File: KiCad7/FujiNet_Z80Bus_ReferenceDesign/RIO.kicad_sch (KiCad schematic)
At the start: 17 parts, among them IC1 7432N, IC2 7404N, IC4 7408N, IC8 7432N, IC9 7408N

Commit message: KiCAD attempt to route a single board (failed)
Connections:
- net DEC14: now also RN1.5; no longer RN1.2
- net DEC15: now also RN1.4; no longer RN1.3
- net DEC_OE: now also RN1.2; no longer RN1.5
- net DEC_WE: now also RN1.3; no longer RN1.4
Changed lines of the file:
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@@
     (effects (font (size 1.27 1.27)) (justify left bottom))
   )
-  (label "DEC_WE" (at 138.43 172.72 180) (fields_autoplaced)
+  (label "DEC_WE" (at 138.43 170.18 180) (fields_autoplaced)
     (effects (font (size 1.27 1.27)) (justify right bottom))
   )
@@
     (effects (font (size 1.27 1.27)) (justify left bottom))
   )
-  (label "DEC15" (at 138.43 170.18 180) (fields_autoplaced)
+  (label "DEC15" (at 138.43 172.72 180) (fields_autoplaced)
     (effects (font (size 1.27 1.27)) (justify right bottom))
   )
@@
     (effects (font (size 1.27 1.27)) (justify right bottom))
   )
-  (label "DEC_OE" (at 138.43 175.26 180) (fields_autoplaced)
+  (label "DEC_OE" (at 138.43 167.64 180) (fields_autoplaced)
     (effects (font (size 1.27 1.27)) (justify right bottom))
   )
@@
     (effects (font (size 1.27 1.27)) (justify left bottom))
   )
-  (label "DEC14" (at 138.43 167.64 180) (fields_autoplaced)
+  (label "DEC14" (at 138.43 175.26 180) (fields_autoplaced)
     (effects (font (size 1.27 1.27)) (justify right bottom))
   )
@@
     (pin "7")
     (instances
-      (project "FujiNet_Z80Bus_Reference"
+      (project "FujiNet_Z80Bus_ReferenceDesign"
         (path "/532c0392-800e-45cc-8170-6d32f2390e83/00000000-0000-0000-0000-0000ad721c5e"
           (reference "IC2") (unit 5)
@@
     (pin "7")
     (instances
-      (project "FujiNet_Z80Bus_Reference"
+      (project "FujiNet_Z80Bus_ReferenceDesign"
         (path "/532c0392-800e-45cc-8170-6d32f2390e83/00000000-0000-0000-0000-0000ad721c5e"
           (reference "IC1") (unit 3)
@@
     (pin "7")
     (instances
-      (project "FujiNet_Z80Bus_Reference"
+      (project "FujiNet_Z80Bus_ReferenceDesign"
         (path "/532c0392-800e-45cc-8170-6d32f2390e83/00000000-0000-0000-0000-0000ad721c5e"
           (reference "IC4") (unit 2)
@@
     (pin "2")
     (instances
-      (project "FujiNet_Z80Bus_Reference"
+      (project "FujiNet_Z80Bus_ReferenceDesign"
         (path "/532c0392-800e-45cc-8170-6d32f2390e83/00000000-0000-0000-0000-0000ad721c5e"
           (reference "R10") (unit 1)
@@
     (pin "1")
     (instances
-      (project "FujiNet_Z80Bus_Reference"
+      (project "FujiNet_Z80Bus_ReferenceDesign"
         (path "/532c0392-800e-45cc-8170-6d32f2390e83/00000000-0000-0000-0000-0000ad721c5e"
           (reference "#PWR023") (unit 1)
@@
     (pin "20")
     (instances
-      (project "FujiNet_Z80Bus_Reference"
+      (project "FujiNet_Z80Bus_ReferenceDesign"
         (path "/532c0392-800e-45cc-8170-6d32f2390e83/00000000-0000-0000-0000-0000ad721c5e"
           (reference "RIO_DECODER1") (unit 1)
@@
     (pin "2")
     (instances
-      (project "FujiNet_Z80Bus_Reference"
+      (project "FujiNet_Z80Bus_ReferenceDesign"
         (path "/532c0392-800e-45cc-8170-6d32f2390e83/00000000-0000-0000-0000-0000ad721c5e"
           (reference "R7") (unit 1)
@@
     (pin "2")
     (instances
-      (project "FujiNet_Z80Bus_Reference"
+      (project "FujiNet_Z80Bus_ReferenceDesign"
         (path "/532c0392-800e-45cc-8170-6d32f2390e83/00000000-0000-0000-0000-0000ad721c5e"
           (reference "R6") (unit 1)
@@
     (pin "3")
     (instances
-      (project "FujiNet_Z80Bus_Reference"
+      (project "FujiNet_Z80Bus_ReferenceDesign"
         (path "/532c0392-800e-45cc-8170-6d32f2390e83/00000000-0000-0000-0000-0000ae2cbb6b"
           (reference "Q?") (unit 1)
@@
     (pin "2")
     (instances
-      (project "FujiNet_Z80Bus_Reference"
+      (project "FujiNet_Z80Bus_ReferenceDesign"
         (path "/532c0392-800e-45cc-8170-6d32f2390e83/00000000-0000-0000-0000-0000ae2cbb6b"
           (reference "R?") (unit 1)
@@
     (pin "2")
     (instances
-      (project "FujiNet_Z80Bus_Reference"
+      (project "FujiNet_Z80Bus_ReferenceDesign"
         (path "/532c0392-800e-45cc-8170-6d32f2390e83/00000000-0000-0000-0000-0000ae2cbb6b"
           (reference "R?") (unit 1)
@@
     (pin "1")
     (instances
-      (project "FujiNet_Z80Bus_Reference"
+      (project "FujiNet_Z80Bus_ReferenceDesign"
         (path "/532c0392-800e-45cc-8170-6d32f2390e83/00000000-0000-0000-0000-0000ad721c5e"
           (reference "#PWR027") (unit 1)
@@
     (pin "20")
     (instances
-      (project "FujiNet_Z80Bus_Reference"
+      (project "FujiNet_Z80Bus_ReferenceDesign"
         (path "/532c0392-800e-45cc-8170-6d32f2390e83/00000000-0000-0000-0000-0000ad721c5e"
           (reference "Z80-RIO_DATA1") (unit 1)
@@
     (pin "9")
     (instances
-      (project "FujiNet_Z80Bus_Reference"
+      (project "FujiNet_Z80Bus_ReferenceDesign"
         (path "/532c0392-800e-45cc-8170-6d32f2390e83/00000000-0000-0000-0000-0000ad721c5e"
           (reference "RIO1") (unit 1)
@@
     (pin "20")
     (instances
-      (project "FujiNet_Z80Bus_Reference"
+      (project "FujiNet_Z80Bus_ReferenceDesign"
         (path "/532c0392-800e-45cc-8170-6d32f2390e83/00000000-0000-0000-0000-0000ad721c5e"
           (reference "RIO_CONTROL1") (unit 1)
@@
     (pin "20")
     (instances
-      (project "FujiNet_Z80Bus_Reference"
+      (project "FujiNet_Z80Bus_ReferenceDesign"
         (path "/532c0392-800e-45cc-8170-6d32f2390e83/00000000-0000-0000-0000-0000ad721c5e"
           (reference "RIO_CONTROL1") (unit 2)
@@
     (pin "7")
     (instances
-      (project "FujiNet_Z80Bus_Reference"
+      (project "FujiNet_Z80Bus_ReferenceDesign"
         (path "/532c0392-800e-45cc-8170-6d32f2390e83/00000000-0000-0000-0000-0000ad721c5e"
           (reference "IC9") (unit 1)
@@
     (pin "7")
     (instances
-      (project "FujiNet_Z80Bus_Reference"
+      (project "FujiNet_Z80Bus_ReferenceDesign"
         (path "/532c0392-800e-45cc-8170-6d32f2390e83/00000000-0000-0000-0000-0000ad721c5e"
           (reference "IC9") (unit 2)
@@
     (pin "7")
     (instances
-      (project "FujiNet_Z80Bus_Reference"
+      (project "FujiNet_Z80Bus_ReferenceDesign"
         (path "/532c0392-800e-45cc-8170-6d32f2390e83/00000000-0000-0000-0000-0000ad721c5e"
           (reference "IC9") (unit 3)
@@
     (pin "7")
     (instances
-      (project "FujiNet_Z80Bus_Reference"
+      (project "FujiNet_Z80Bus_ReferenceDesign"
         (path "/532c0392-800e-45cc-8170-6d32f2390e83/00000000-0000-0000-0000-0000ad721c5e"
           (reference "IC9") (unit 4)
@@
     (pin "7")
     (instances
-      (project "FujiNet_Z80Bus_Reference"
+      (project "FujiNet_Z80Bus_ReferenceDesign"
         (path "/532c0392-800e-45cc-8170-6d32f2390e83/00000000-0000-0000-0000-0000ad721c5e"
           (reference "IC8") (unit 1)
@@
     (pin "7")
     (instances
-      (project "FujiNet_Z80Bus_Reference"
+      (project "FujiNet_Z80Bus_ReferenceDesign"
         (path "/532c0392-800e-45cc-8170-6d32f2390e83/00000000-0000-0000-0000-0000ad721c5e"
           (reference "IC8") (unit 3)
@@
     (pin "7")
     (instances
-      (project "FujiNet_Z80Bus_Reference"
+      (project "FujiNet_Z80Bus_ReferenceDesign"
         (path "/532c0392-800e-45cc-8170-6d32f2390e83/00000000-0000-0000-0000-0000ad721c5e"
           (reference "IC8") (unit 4)
@@
     (pin "7")
     (instances
-      (project "FujiNet_Z80Bus_Reference"
+      (project "FujiNet_Z80Bus_ReferenceDesign"
         (path "/532c0392-800e-45cc-8170-6d32f2390e83/00000000-0000-0000-0000-0000ad721c5e"
           (reference "IC8") (unit 2)
@@
     (pin "9")
     (instances
-      (project "FujiNet_Z80Bus_Reference"
+      (project "FujiNet_Z80Bus_ReferenceDesign"
         (path "/532c0392-800e-45cc-8170-6d32f2390e83/00000000-0000-0000-0000-0000ad721c5e"
           (reference "RN1") (unit 1)
@@
     (pin "2")
     (instances
-      (project "FujiNet_Z80Bus_Reference"
+      (project "FujiNet_Z80Bus_ReferenceDesign"
         (path "/532c0392-800e-45cc-8170-6d32f2390e83/00000000-0000-0000-0000-0000ad721c5e"
           (reference "D16") (unit 1)
@@
     (pin "1")
     (instances
-      (project "FujiNet_Z80Bus_Reference"
+      (project "FujiNet_Z80Bus_ReferenceDesign"
         (path "/532c0392-800e-45cc-8170-6d32f2390e83/00000000-0000-0000-0000-0000ad721c5e"
           (reference "#PWR024") (unit 1)
@@
     (pin "1")
     (instances
-      (project "FujiNet_Z80Bus_Reference"
+      (project "FujiNet_Z80Bus_ReferenceDesign"
         (path "/532c0392-800e-45cc-8170-6d32f2390e83/00000000-0000-0000-0000-0000ad721c5e"
           (reference "#PWR026") (unit 1)
@@
     (pin "1")
     (instances
-      (project "FujiNet_Z80Bus_Reference"
+      (project "FujiNet_Z80Bus_ReferenceDesign"
         (path "/532c0392-800e-45cc-8170-6d32f2390e83/00000000-0000-0000-0000-0000ad721c5e"
           (reference "#PWR022") (unit 1)
@@
     (pin "1")
     (instances
-      (project "FujiNet_Z80Bus_Reference"
+      (project "FujiNet_Z80Bus_ReferenceDesign"
         (path "/532c0392-800e-45cc-8170-6d32f2390e83/00000000-0000-0000-0000-0000ad721c5e"
           (reference "#PWR028") (unit 1)
@@
     (pin "1")
     (instances
-      (project "FujiNet_Z80Bus_Reference"
+      (project "FujiNet_Z80Bus_ReferenceDesign"
         (path "/532c0392-800e-45cc-8170-6d32f2390e83/00000000-0000-0000-0000-0000ad721c5e"
           (reference "#PWR025") (unit 1)

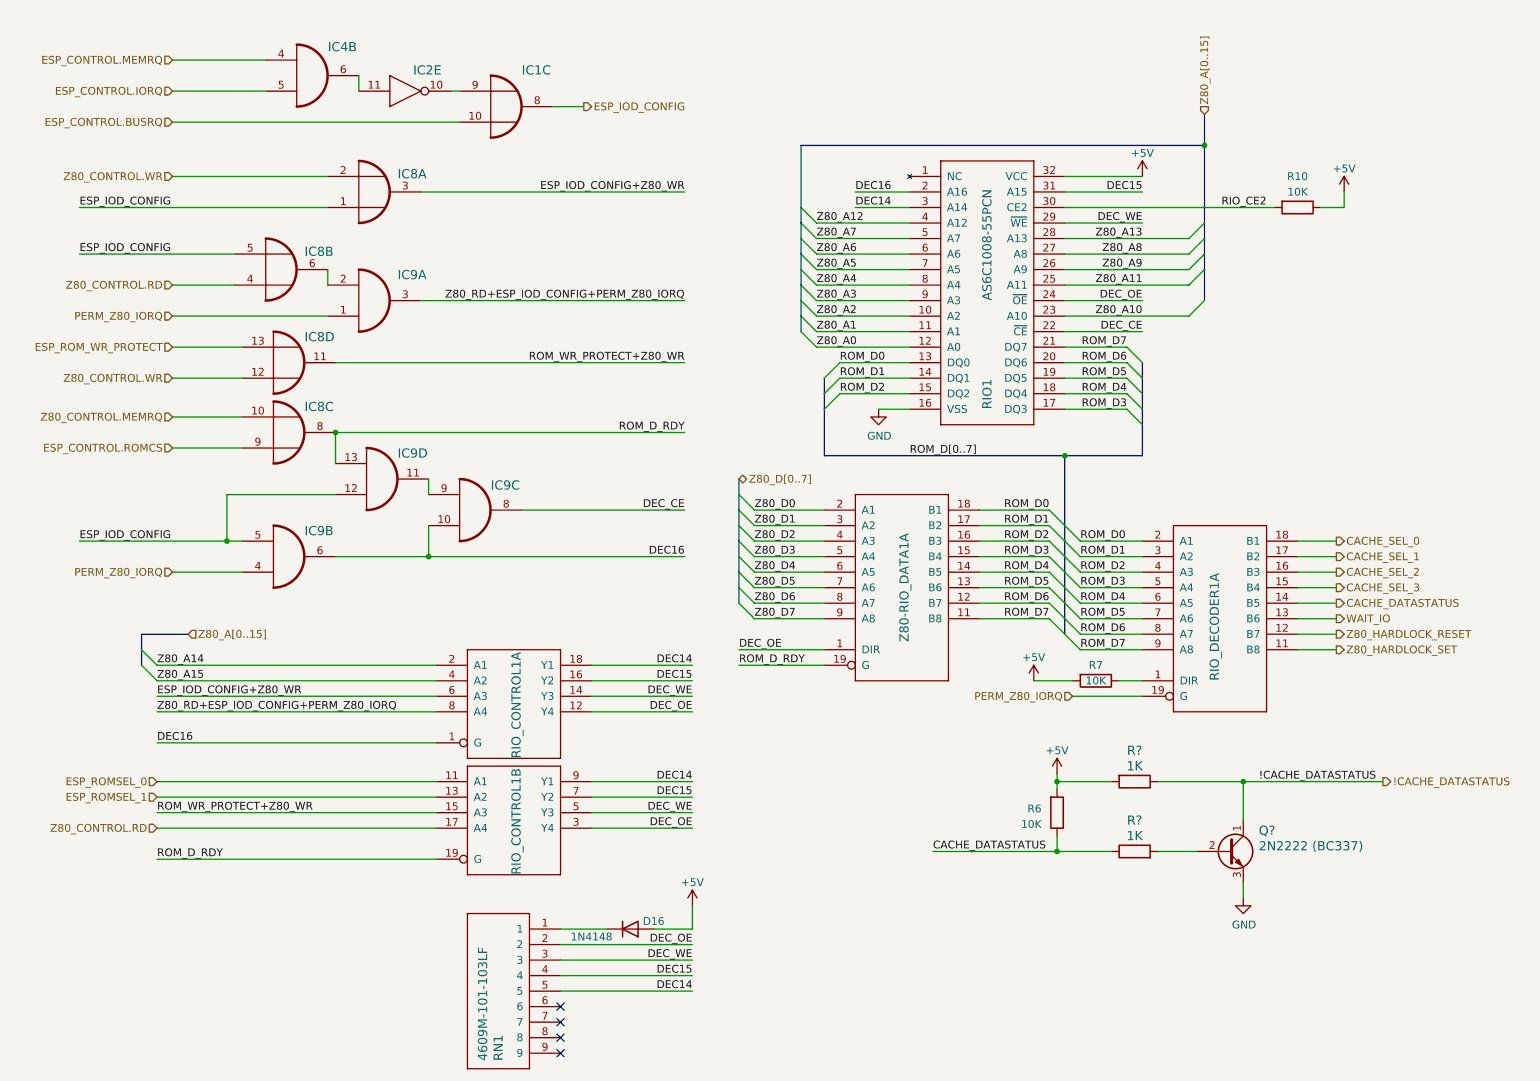
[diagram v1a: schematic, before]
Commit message: KiCad massive refactoring to enable modular PCB design
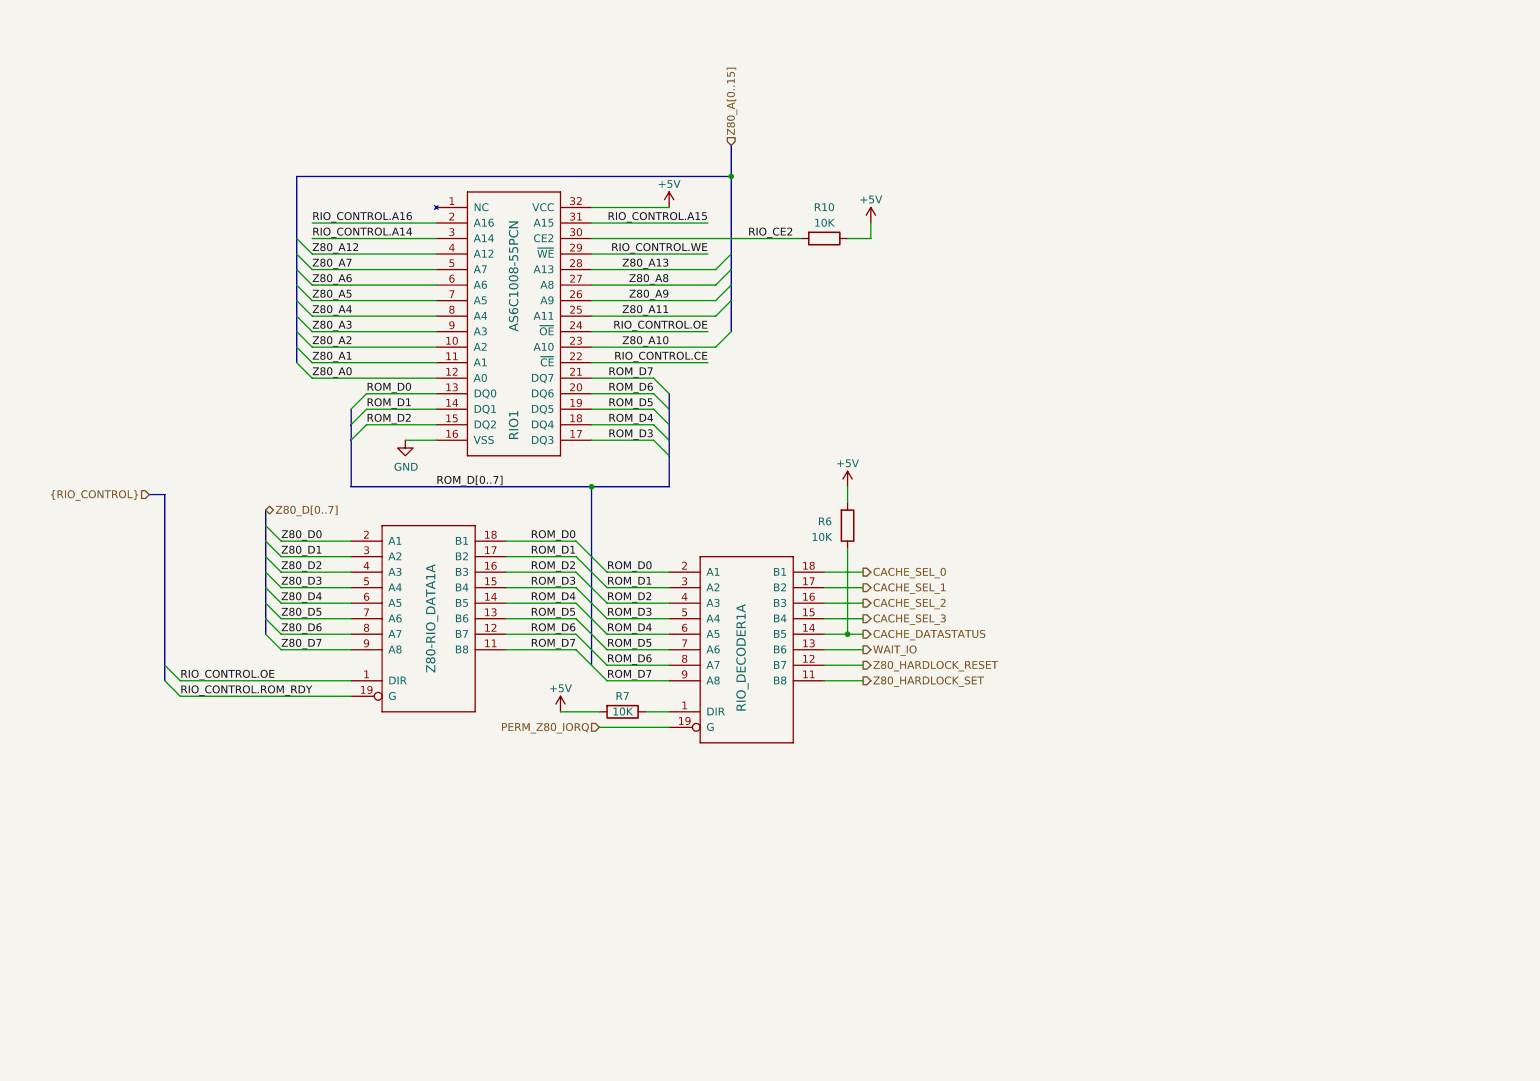
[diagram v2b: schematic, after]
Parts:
- removed D16: 1N4148, Diode_THT:D_T-1_P5.08mm_Horizontal, symbol Device:D
- removed IC1: 7432N, Package_DIP:DIP-14_W7.62mm_Socket, symbol FujiNet_Z80Bus_Reference-rescue:7432N-Z80ESP-eagle-import
- removed IC2: 7404N, Package_DIP:DIP-14_W7.62mm_Socket, symbol FujiNet_Z80Bus_Reference-rescue:7404N-Z80ESP-eagle-import
- removed IC4: 7408N, Package_DIP:DIP-14_W7.62mm_Socket, symbol FujiNet_Z80Bus_Reference-rescue:7408N-Z80ESP-eagle-import
- removed IC8: 7432N, Package_DIP:DIP-14_W7.62mm_Socket, symbol FujiNet_Z80Bus_Reference-rescue:7432N-Z80Decoder-eagle-import
- removed IC9: 7408N, Package_DIP:DIP-14_W7.62mm_Socket, symbol FujiNet_Z80Bus_Reference-rescue:7408N-Z80Decoder-eagle-import
- removed Q?: 2N2222 (BC337), Package_TO_SOT_THT:TO-92, symbol Transistor_BJT:BC337
- removed R? (x2): 1K, Resistor_THT:R_Axial_DIN0207_L6.3mm_D2.5mm_P10.16mm_Horizontal, symbol Device:R
- removed RIO_CONTROL1: 74244N, Package_DIP:DIP-20_W7.62mm_Socket, symbol FujiNet_Z80Bus_Reference-rescue:74244N-Z80Decoder-eagle-import
- removed RN1: 4609M-101-103LF, Resistor_THT:R_Array_SIP9, symbol FujiNet_Z80Bus_Reference-rescue:4609M-101-103LF-Z80Decoder-eagle-import
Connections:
- net DEC14 renamed RIO_CONTROL.A14
- net DEC15 renamed RIO_CONTROL.A15
- net DEC16 renamed RIO_CONTROL.A16
- net DEC_CE renamed RIO_CONTROL.CE
- net DEC_OE renamed RIO_CONTROL.OE
- net DEC_WE renamed RIO_CONTROL.WE
- net ROM_D_RDY renamed RIO_CONTROL.ROM_RDY
- no-connect marks 4 -> 0
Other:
- moved on the sheet: R10, R7, RIO1, RIO_DECODER1A, Z80-RIO_DATA1A
